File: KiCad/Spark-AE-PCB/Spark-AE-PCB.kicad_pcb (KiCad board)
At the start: 2 copper layers, 50 x 100 mm, 162 parts, among them CN1 I2C_IN, CN2 I2C_OUT, J1 Conn_01x20_Socket, J2 Conn_01x20_Socket, J3 AE_BUS, J4 Inputs, J5 Outputs, J6 SPI, J7 SD_CONN, Q1 AO3401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

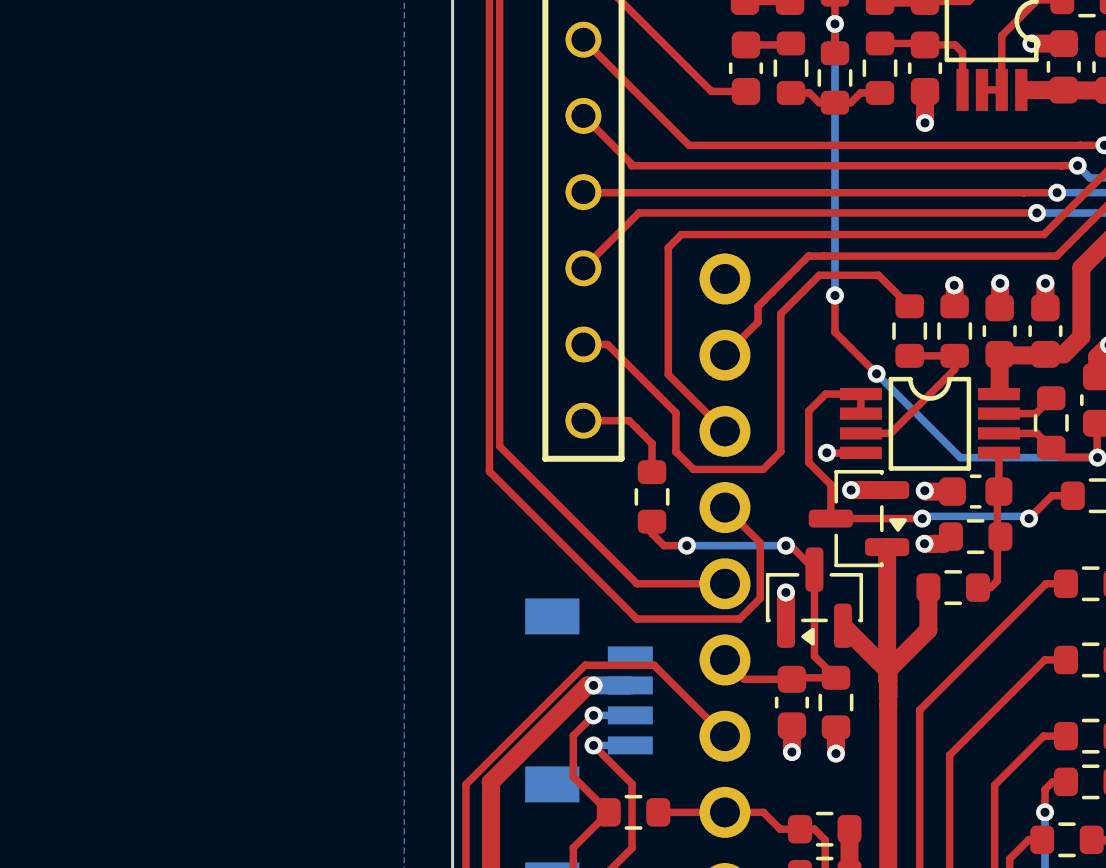
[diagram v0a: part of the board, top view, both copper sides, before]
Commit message: bumped version to Mk0.1 and corrected polarity of D4 on schematic
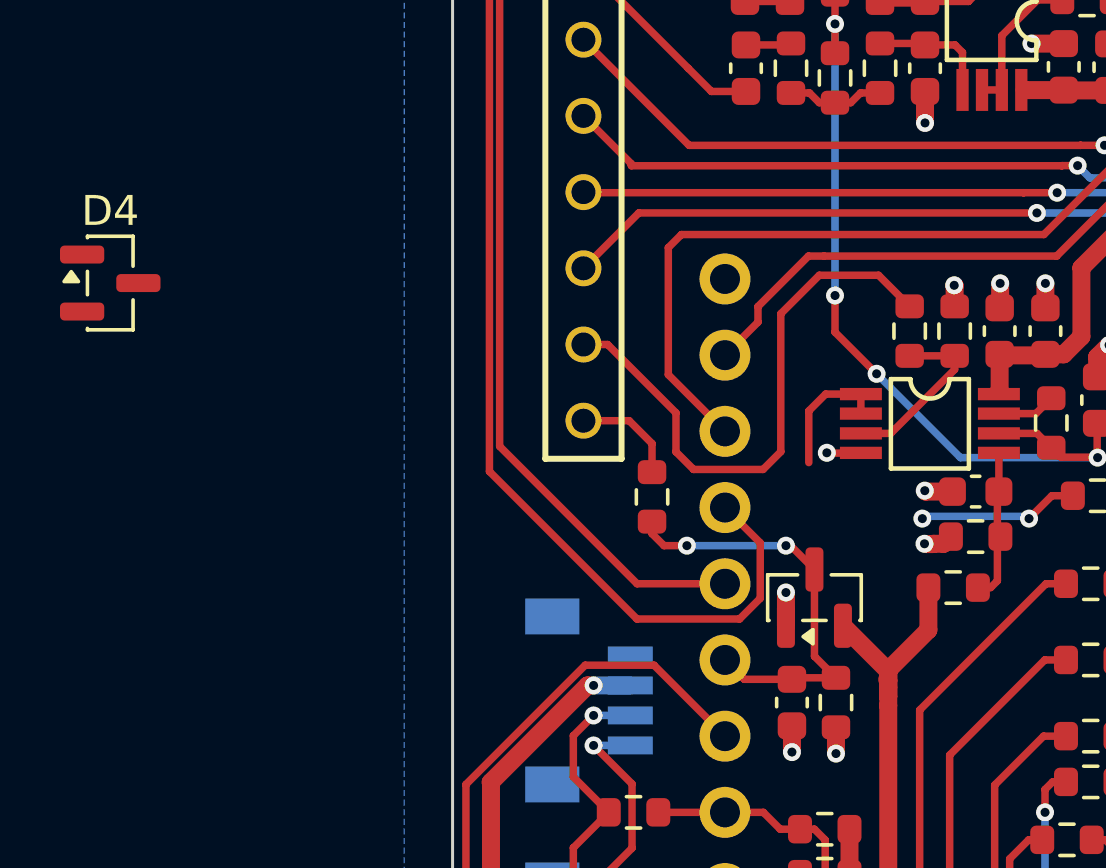
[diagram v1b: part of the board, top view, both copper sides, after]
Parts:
- moved D4 26.2 mm to (67.0, 63.5), turned to 0 degrees
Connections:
- D4 pad 1: +3.3V -> GND
- D4 pad 2: GND -> +3.3V
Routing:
- net Net-(D4-COM): track 15.0 -> 9.74 mm
- net +3.3V: track 262.0 -> 257.5 mm
- net GND: track 108.6 -> 107.4 mm, vias 70 -> 69
